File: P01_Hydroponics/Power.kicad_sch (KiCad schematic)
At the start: 39 parts, among them Q5 PMOS, U3 TPSM33625RDNR, U4 TPSM33625RDNR, U5 BQ25306

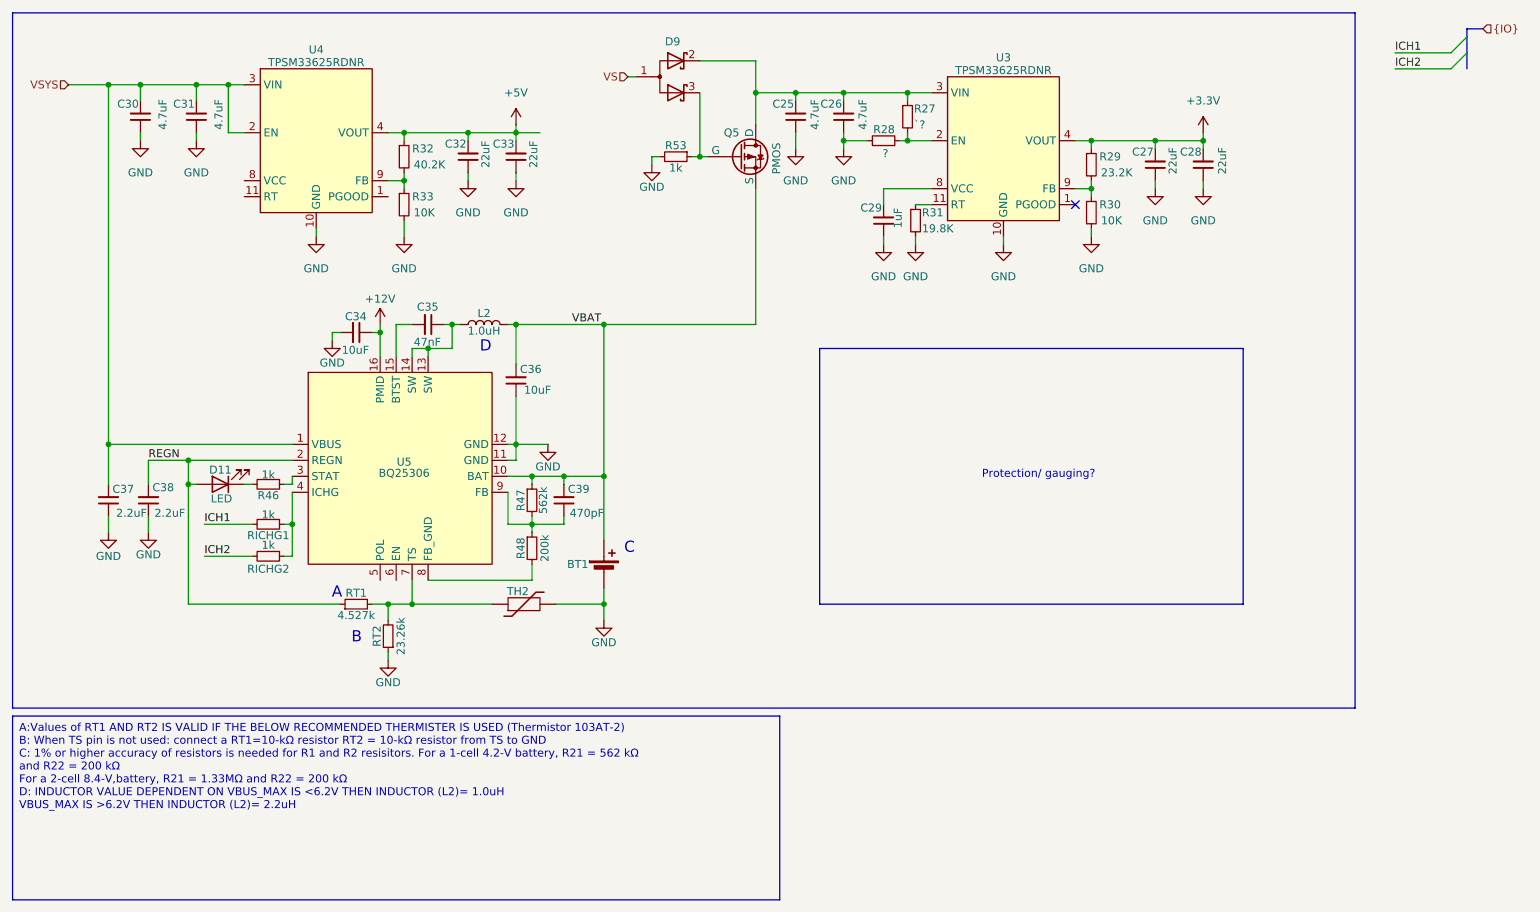
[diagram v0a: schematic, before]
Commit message: Need review
Updated:
STD14 to tag connect.
Added most footprints.
Change crystal to oscillator for ESP32
Rearrange radio controller schematic.
Added NOR flash.
Added USB-C connector for ESP32
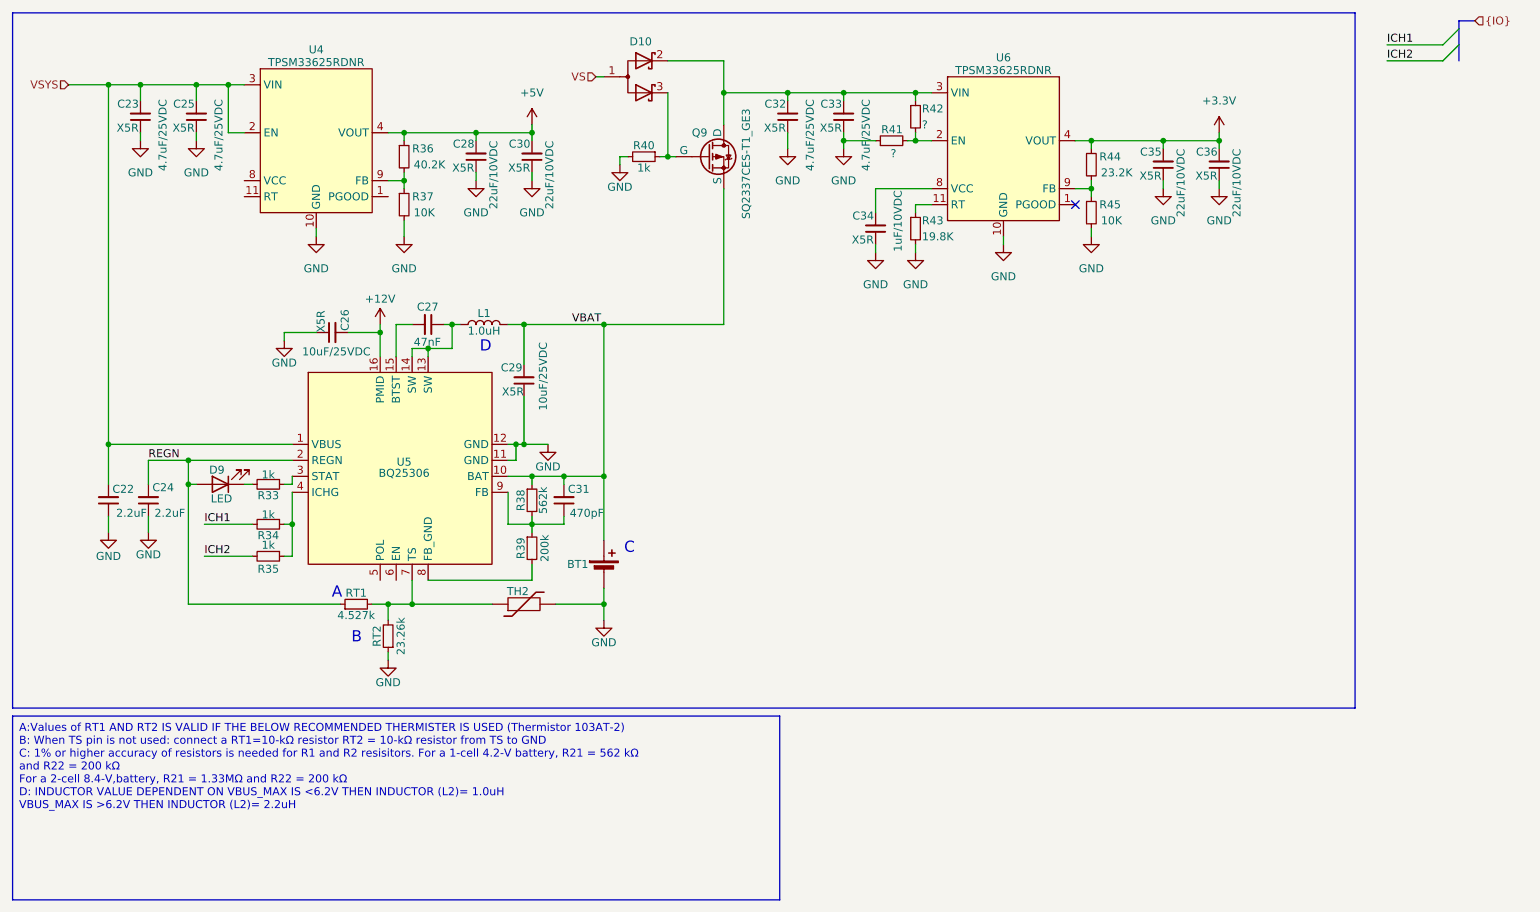
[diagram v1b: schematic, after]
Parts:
- removed C27, C28: 22uF, symbol Device:C_Small
- removed C31: 4.7uF, symbol Device:C_Small
- added C23, C32: 4.7uF/25VDC, Capacitor_SMD:C_0603_1608Metric_Pad1.08x0.95mm_HandSolder, symbol Device:C_Small
- added C35: 22uF/10VDC, Capacitor_SMD:C_0603_1608Metric_Pad1.08x0.95mm_HandSolder, symbol Device:C_Small
- BT1: footprint (none) -> Connector_PinHeader_1.00mm:PinHeader_1x02_P1.00mm_Vertical
- C22: renamed from C37; footprint (none) -> Capacitor_SMD:C_0603_1608Metric_Pad1.08x0.95mm_HandSolder
- C24: renamed from C38; footprint (none) -> Capacitor_SMD:C_0603_1608Metric_Pad1.08x0.95mm_HandSolder
- C25: value 4.7uF -> 4.7uF/25VDC; footprint (none) -> Capacitor_SMD:C_0603_1608Metric_Pad1.08x0.95mm_HandSolder; Dielelectric (none) -> X5R
- C26: value 4.7uF -> 10uF/25VDC; footprint (none) -> Capacitor_SMD:C_0603_1608Metric_Pad1.08x0.95mm_HandSolder; Dielectric (none) -> X5R
- C27: renamed from C35; footprint (none) -> Capacitor_SMD:C_0603_1608Metric_Pad1.08x0.95mm_HandSolder
- C28: renamed from C32; value 22uF -> 22uF/10VDC; footprint (none) -> Capacitor_SMD:C_0603_1608Metric_Pad1.08x0.95mm_HandSolder; Dielectric (none) -> X5R
- C29: value 1uF -> 10uF/25VDC; footprint (none) -> Capacitor_SMD:C_0603_1608Metric_Pad1.08x0.95mm_HandSolder; Dielectric (none) -> X5R
- C30: value 4.7uF -> 22uF/10VDC; footprint (none) -> Capacitor_SMD:C_0603_1608Metric_Pad1.08x0.95mm_HandSolder; Dielectric (none) -> X5R
- C31: renamed from C39; footprint (none) -> Capacitor_SMD:C_0603_1608Metric_Pad1.08x0.95mm_HandSolder
- C33: value 22uF -> 4.7uF/25VDC; footprint (none) -> Capacitor_SMD:C_0603_1608Metric_Pad1.08x0.95mm_HandSolder; Dielelectric (none) -> X5R
- C34: value 10uF -> 1uF/10VDC; footprint (none) -> Capacitor_SMD:C_0603_1608Metric_Pad1.08x0.95mm_HandSolder; Dielectric (none) -> X5R
- C36: value 10uF -> 22uF/10VDC; footprint (none) -> Capacitor_SMD:C_0603_1608Metric_Pad1.08x0.95mm_HandSolder; Dielectric (none) -> X5R
- D9: renamed from D11; footprint (none) -> LED_SMD:LED_0603_1608Metric_Pad1.05x0.95mm_HandSolder
- Q9: renamed from Q5; value PMOS -> SQ2337CES-T1_GE3; footprint (none) -> Package_TO_SOT_SMD:SOT-23-3
- R33: renamed from R46; footprint (none) -> Resistor_SMD:R_0603_1608Metric_Pad0.98x0.95mm_HandSolder
- R34: renamed from RICHG1; footprint (none) -> Resistor_SMD:R_0603_1608Metric_Pad0.98x0.95mm_HandSolder
- R35: renamed from RICHG2; footprint (none) -> Resistor_SMD:R_0603_1608Metric_Pad0.98x0.95mm_HandSolder
- R36: renamed from R32; footprint (none) -> Resistor_SMD:R_0603_1608Metric_Pad0.98x0.95mm_HandSolder
- R37: renamed from R33; footprint (none) -> Resistor_SMD:R_0603_1608Metric_Pad0.98x0.95mm_HandSolder
- R38: renamed from R47; footprint (none) -> Resistor_SMD:R_0603_1608Metric_Pad0.98x0.95mm_HandSolder
- R39: renamed from R48; footprint (none) -> Resistor_SMD:R_0603_1608Metric_Pad0.98x0.95mm_HandSolder
- R40: renamed from R53; footprint (none) -> Resistor_SMD:R_0603_1608Metric_Pad0.98x0.95mm_HandSolder
- R41: renamed from R28; footprint (none) -> Resistor_SMD:R_0603_1608Metric_Pad0.98x0.95mm_HandSolder
- R42: renamed from R27; value `? -> ?; footprint (none) -> Resistor_SMD:R_0603_1608Metric_Pad0.98x0.95mm_HandSolder
- R43: renamed from R31; footprint (none) -> Resistor_SMD:R_0603_1608Metric_Pad0.98x0.95mm_HandSolder
- R44: renamed from R29; footprint (none) -> Resistor_SMD:R_0603_1608Metric_Pad0.98x0.95mm_HandSolder
- R45: renamed from R30; footprint (none) -> Resistor_SMD:R_0603_1608Metric_Pad0.98x0.95mm_HandSolder
- RT1, RT2: footprint (none) -> Resistor_SMD:R_0603_1608Metric_Pad0.98x0.95mm_HandSolder
- U4: footprint (none) -> TPSM33625RDNR:CONV_TLVM23615RDNR
- U6: renamed from U3; footprint (none) -> TPSM33625RDNR:CONV_TLVM23615RDNR
- renumbered D9 to D10, L2 to L1
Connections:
- net +12V: now also C26.2; no longer C34.1
- net +3.3V: now also C36.2, C35.2
- net +5V: now also C30.2; no longer C33.2
- net GND: now also C34.1, C23.1, C32.1, C35.1; no longer C34.2
- net VBAT: now also C29.2; no longer C36.2
- net VSYS: now also C25.2, C23.2; no longer C30.2
- net at D10.2 (K), Q9.1 (D), R42.1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: now also C33.2, C32.2; no longer C25.2, C26.2
- net at U6.8 (VCC): now also C34.2; no longer C29.2
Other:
- note removed: "Protection/ gauging?"
- moved on the sheet: C28, D10, Q9, R40, R41, R42, R43
